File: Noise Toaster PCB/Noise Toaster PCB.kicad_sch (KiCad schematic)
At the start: 0 parts

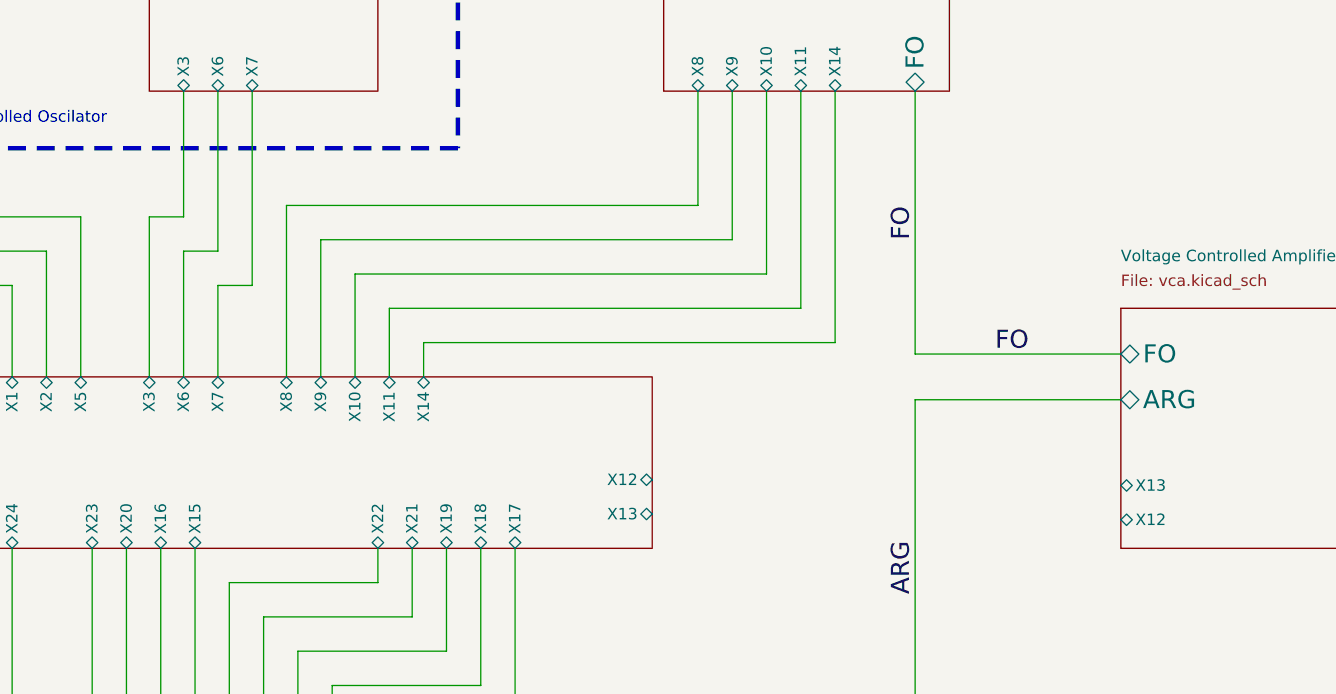
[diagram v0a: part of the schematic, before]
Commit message: wireing and components have been checked
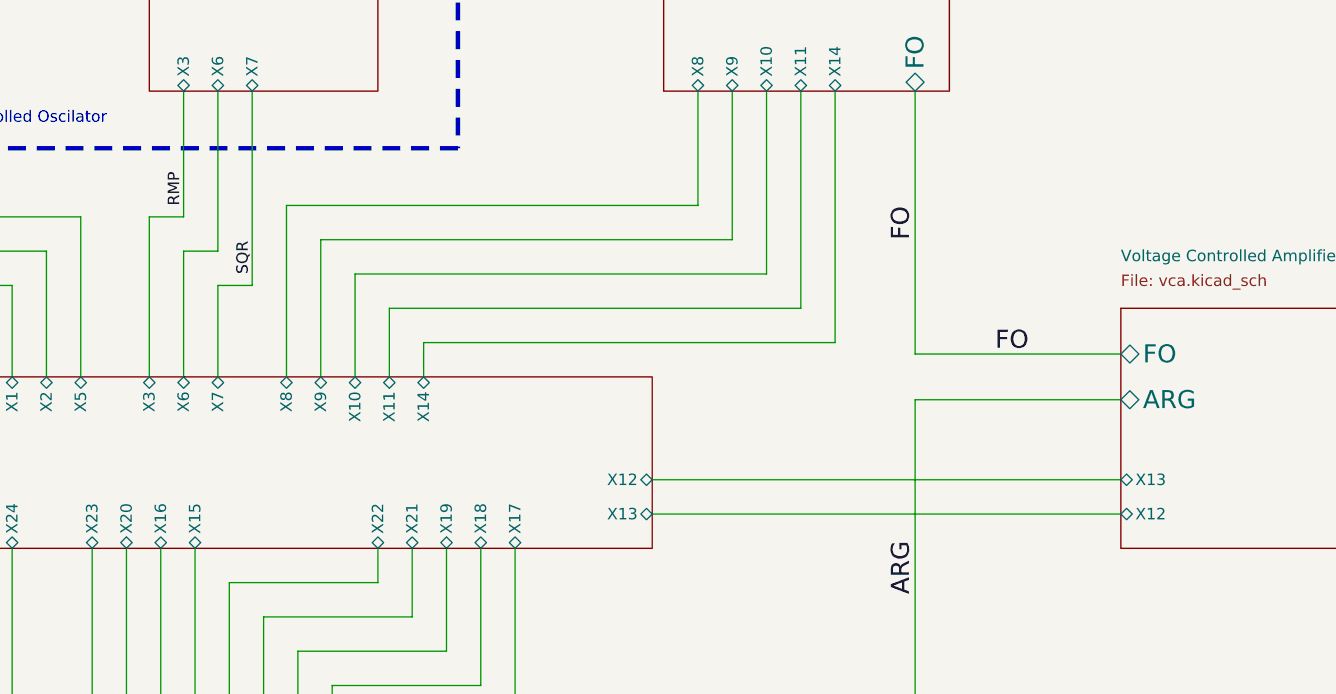
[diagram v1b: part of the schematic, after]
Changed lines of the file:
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@@
     (stroke (width 0) (type default) (color 255 157 0 1))
+  )
+  (wire (pts (xy 189.23 110.49) (xy 241.3 110.49))
+    (stroke (width 0) (type default))
   )
   (wire (pts (xy 114.3 114.3) (xy 114.3 128.27))
     (stroke (width 0) (type default) (color 255 157 0 1))
   )
+  (wire (pts (xy 144.78 63.5) (xy 144.78 85.09))
+    (stroke (width 0) (type default) (color 255 157 0 1))
+  )
   (wire (pts (xy 110.49 124.46) (xy 39.37 124.46))
     (stroke (width 0) (type default) (color 255 157 0 1))
@@
   (wire (pts (xy 194.31 76.2) (xy 194.31 63.5))
     (stroke (width 0) (type default) (color 255 157 0 1))
+  )
+  (wire (pts (xy 189.23 106.68) (xy 241.3 106.68))
+    (stroke (width 0) (type default))
   )
   (wire (pts (xy 205.74 63.5) (xy 205.74 87.63))
@@
   )
   (wire (pts (xy 127 135.89) (xy 86.36 135.89))
-    (stroke (width 0) (type default) (color 255 157 0 1))
-  )
-  (wire (pts (xy 144.78 63.5) (xy 144.78 85.09))
     (stroke (width 0) (type default) (color 255 157 0 1))
   )
@@
     (effects (font (size 2 2)) (justify left bottom))
   )
+  (label "RMP" (at 137.16 76.2 90) (fields_autoplaced)
+    (effects (font (size 1.27 1.27)) (justify left bottom))
+  )
   (label "G2" (at 118.1569 33.8641 0) (fields_autoplaced)
     (effects (font (size 2 2)) (justify left bottom))
@@
   (label "FO" (at 227.33 92.71 0) (fields_autoplaced)
     (effects (font (size 2 2)) (justify left bottom))
+  )
+  (label "SQR" (at 144.78 83.82 90) (fields_autoplaced)
+    (effects (font (size 1.27 1.27)) (justify left bottom))
   )
   (sheet (at 133.35 152.4) (size 31.75 38.1)
@@
       (effects (font (size 2 2)) (justify left))
     )
-    (pin "X13" bidirectional (at 241.3 107.315 180)
-      (effects (font (size 1.27 1.27)) (justify left))
-    )
-    (pin "X12" bidirectional (at 241.3 111.125 180)
-      (effects (font (size 1.27 1.27)) (justify left))
-    )
+    (pin "X13" bidirectional (at 241.3 106.68 180)
+      (effects (font (size 1.27 1.27)) (justify left))
+    )
+    (pin "X12" bidirectional (at 241.3 110.49 180)
+      (effects (font (size 1.27 1.27)) (justify left))
+    )

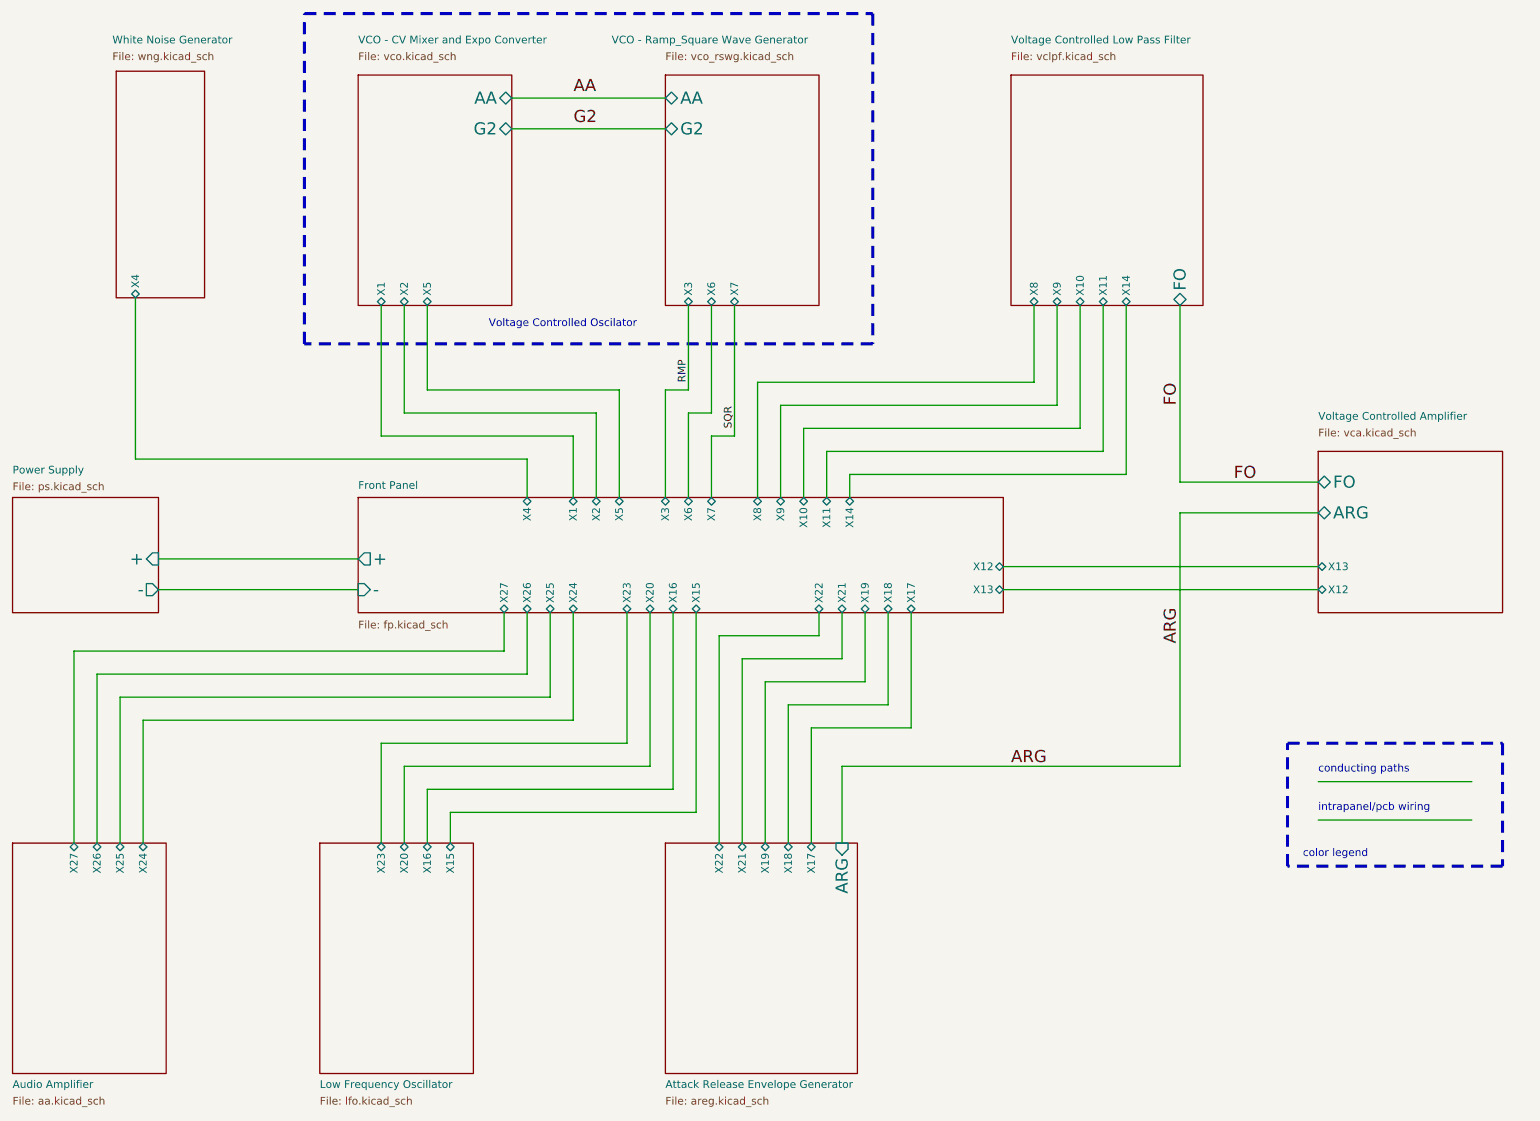
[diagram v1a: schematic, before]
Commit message: applied footprints
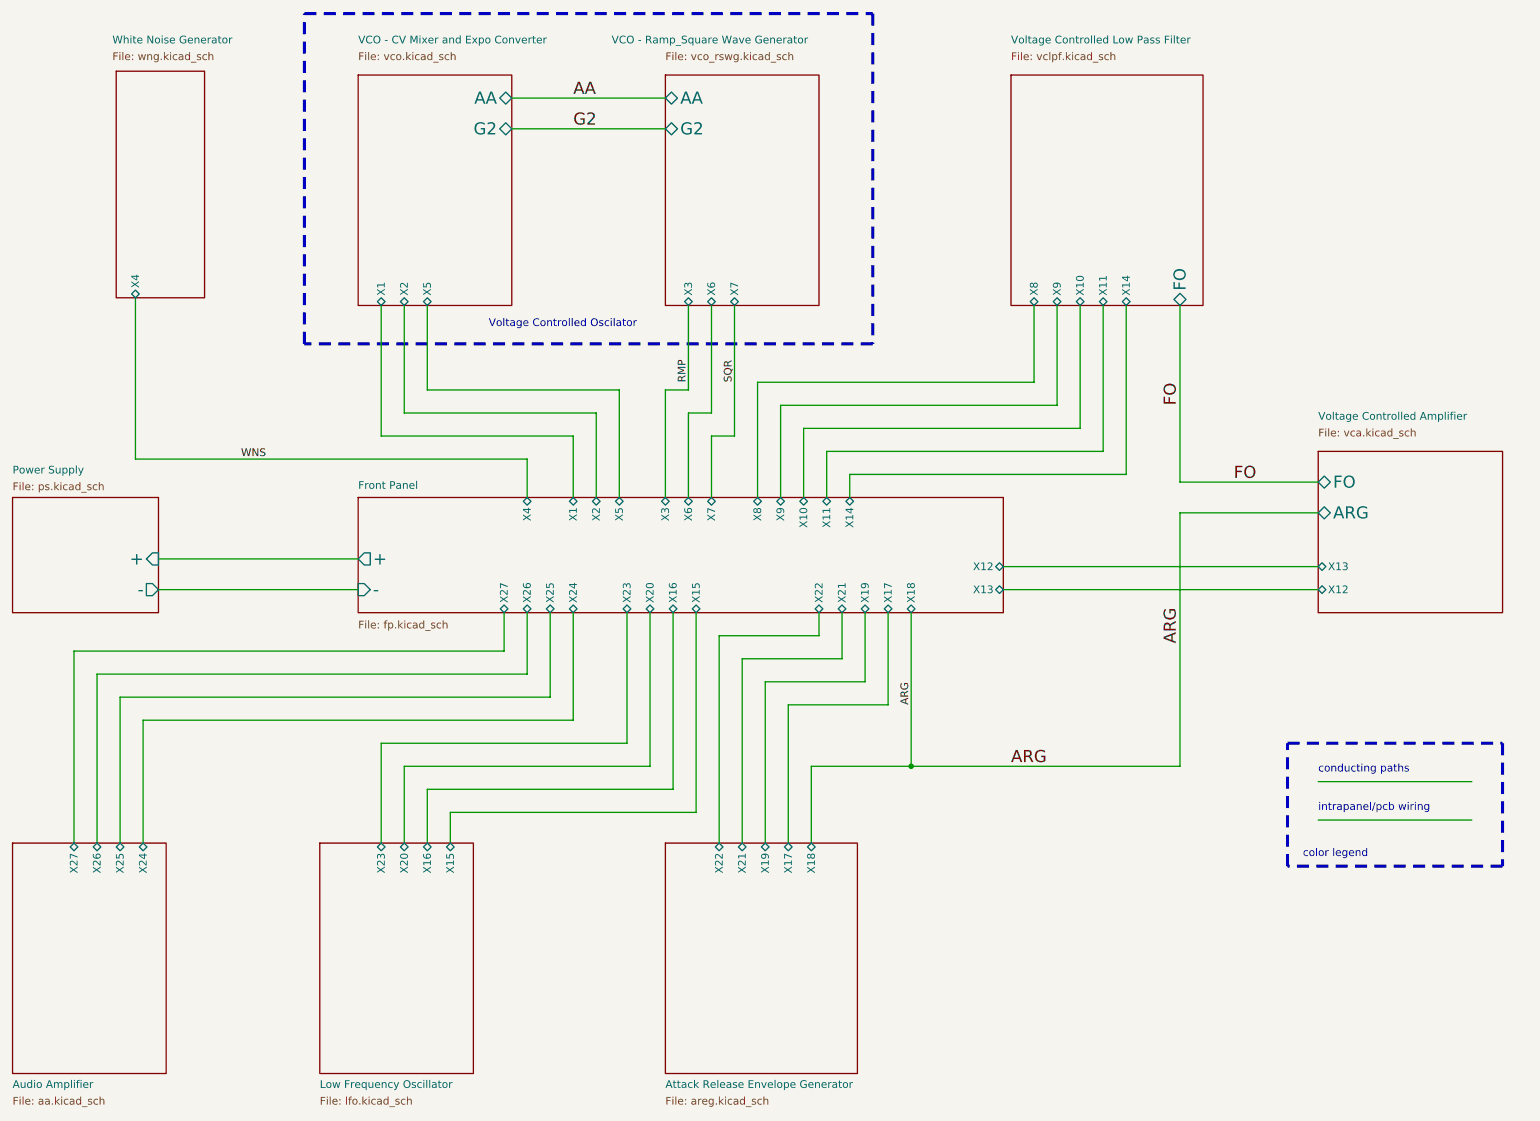
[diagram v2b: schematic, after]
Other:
- sheet Attack Release Envelope Generator ports: added none; removed ARG
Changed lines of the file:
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@@
     (comment 3 "Music From Outer Space LLC")
   )
+  (junction (at 173.99 139.7) (diameter 0) (color 0 0 0 0)
+  )
   (wire (pts (xy 114.3 128.27) (xy 43.18 128.27))
     (stroke (width 0) (type default) (color 255 157 0 1))
@@
     (stroke (width 0) (type default) (color 255 157 0 1))
   )
+  (wire (pts (xy 156.21 95.25) (xy 156.21 83.82))
+    (stroke (width 0) (type default) (color 255 157 0 1))
+  )
+  (wire (pts (xy 86.36 63.5) (xy 86.36 85.09))
+    (stroke (width 0) (type default) (color 255 157 0 1))
+  )
+  (wire (pts (xy 138.43 147.32) (xy 97.79 147.32))
+    (stroke (width 0) (type default) (color 255 157 0 1))
+  )
+  (wire (pts (xy 163.83 91.44) (xy 163.83 95.25))
+    (stroke (width 0) (type default) (color 255 157 0 1))
+  )
+  (wire (pts (xy 90.17 81.28) (xy 121.92 81.28))
+    (stroke (width 0) (type default) (color 255 157 0 1))
+  )
+  (wire (pts (xy 107.95 29.21) (xy 133.35 29.21))
+    (stroke (width 0) (type default))
+  )
+  (wire (pts (xy 173.99 139.7) (xy 218.44 139.7))
+    (stroke (width 0) (type default))
+  )
   (wire (pts (xy 153.67 129.54) (xy 153.67 152.4))
     (stroke (width 0) (type default) (color 255 157 0 1))
   )
-  (wire (pts (xy 156.21 95.25) (xy 156.21 83.82))
-    (stroke (width 0) (type default) (color 255 157 0 1))
-  )
-  (wire (pts (xy 86.36 63.5) (xy 86.36 85.09))
-    (stroke (width 0) (type default) (color 255 157 0 1))
-  )
-  (wire (pts (xy 138.43 147.32) (xy 97.79 147.32))
-    (stroke (width 0) (type default) (color 255 157 0 1))
-  )
-  (wire (pts (xy 163.83 91.44) (xy 163.83 95.25))
-    (stroke (width 0) (type default) (color 255 157 0 1))
-  )
-  (wire (pts (xy 90.17 81.28) (xy 121.92 81.28))
-    (stroke (width 0) (type default) (color 255 157 0 1))
-  )
-  (wire (pts (xy 107.95 29.21) (xy 133.35 29.21))
-    (stroke (width 0) (type default))
-  )
-  (wire (pts (xy 157.48 133.35) (xy 157.48 152.4))
-    (stroke (width 0) (type default) (color 255 157 0 1))
-  )
   (wire (pts (xy 130.81 114.3) (xy 130.81 139.7))
     (stroke (width 0) (type default) (color 255 157 0 1))
@@
     (stroke (width 0) (type default) (color 255 157 0 1))
   )
-  (wire (pts (xy 162.56 139.7) (xy 218.44 139.7))
+  (wire (pts (xy 157.48 139.7) (xy 173.99 139.7))
     (stroke (width 0) (type default))
   )
@@
     (stroke (width 0) (type default) (color 255 157 0 1))
   )
-  (wire (pts (xy 173.99 133.35) (xy 157.48 133.35))
+  (wire (pts (xy 170.18 129.54) (xy 153.67 129.54))
     (stroke (width 0) (type default) (color 255 157 0 1))
   )
@@
     (stroke (width 0) (type default) (color 255 157 0 1))
   )
-  (wire (pts (xy 173.99 114.3) (xy 173.99 133.35))
+  (wire (pts (xy 170.18 114.3) (xy 170.18 129.54))
     (stroke (width 0) (type default) (color 255 157 0 1))
   )
   (wire (pts (xy 189.23 110.49) (xy 241.3 110.49))
-    (stroke (width 0) (type default))
+    (stroke (width 0) (type default) (color 255 157 0 1))
   )
   (wire (pts (xy 114.3 114.3) (xy 114.3 128.27))
     (stroke (width 0) (type default) (color 255 157 0 1))
   )
+  (wire (pts (xy 110.49 124.46) (xy 39.37 124.46))
+    (stroke (width 0) (type default) (color 255 157 0 1))
+  )
+  (wire (pts (xy 146.05 121.92) (xy 146.05 152.4))
+    (stroke (width 0) (type default) (color 255 157 0 1))
+  )
   (wire (pts (xy 144.78 63.5) (xy 144.78 85.09))
     (stroke (width 0) (type default) (color 255 157 0 1))
   )
-  (wire (pts (xy 110.49 124.46) (xy 39.37 124.46))
-    (stroke (width 0) (type default) (color 255 157 0 1))
-  )
-  (wire (pts (xy 146.05 121.92) (xy 146.05 152.4))
-    (stroke (width 0) (type default) (color 255 157 0 1))
-  )
   (wire (pts (xy 134.62 143.51) (xy 93.98 143.51))
     (stroke (width 0) (type default) (color 255 157 0 1))
@@
   )
   (wire (pts (xy 189.23 106.68) (xy 241.3 106.68))
-    (stroke (width 0) (type default))
+    (stroke (width 0) (type default) (color 255 157 0 1))
   )
   (wire (pts (xy 205.74 63.5) (xy 205.74 87.63))
@@
     (stroke (width 0) (type default) (color 255 157 0 1))
   )
-  (wire (pts (xy 162.56 139.7) (xy 162.56 152.4))
-    (stroke (width 0) (type default))
-  )
   (wire (pts (xy 43.18 128.27) (xy 43.18 152.4))
     (stroke (width 0) (type default) (color 255 157 0 1))
@@
     (stroke (width 0) (type default) (color 255 157 0 1))
   )
-  (wire (pts (xy 170.18 129.54) (xy 153.67 129.54))
-    (stroke (width 0) (type default) (color 255 157 0 1))
-  )
   (wire (pts (xy 241.3 92.71) (xy 218.44 92.71))
     (stroke (width 0) (type default))
@@
     (stroke (width 0) (type default) (color 255 157 0 1))
   )
+  (wire (pts (xy 157.48 139.7) (xy 157.48 152.4))
+    (stroke (width 0) (type default))
+  )
   (wire (pts (xy 148.59 95.25) (xy 148.59 76.2))
     (stroke (width 0) (type default) (color 255 157 0 1))
@@
     (stroke (width 0) (type default))
   )
-  (wire (pts (xy 170.18 114.3) (xy 170.18 129.54))
+  (wire (pts (xy 173.99 114.3) (xy 173.99 139.7))
     (stroke (width 0) (type default) (color 255 157 0 1))
   )
@@
     (effects (font (size 1.27 1.27)) (justify left bottom))
   )
-  (label "G2" (at 118.1569 33.8641 0) (fields_autoplaced)
-    (effects (font (size 2 2)) (justify left bottom))
-  )
-  (label "AA" (at 118.1521 28.7399 0) (fields_autoplaced)
+  (label "G2" (at 118.11 34.29 0) (fields_autoplaced)
+    (effects (font (size 2 2)) (justify left bottom))
+  )
+  (label "AA" (at 118.11 29.21 0) (fields_autoplaced)
     (effects (font (size 2 2)) (justify left bottom))
   )
@@
     (effects (font (size 2 2)) (justify left bottom))
   )
-  (label "SQR" (at 144.78 83.82 90) (fields_autoplaced)
-    (effects (font (size 1.27 1.27)) (justify left bottom))
+  (label "SQR" (at 144.78 76.2 90) (fields_autoplaced)
+    (effects (font (size 1.27 1.27)) (justify left bottom))
+  )
+  (label "ARG" (at 173.99 129.54 90) (fields_autoplaced)
+    (effects (font (size 1.27 1.27)) (justify left bottom))
+  )
+  (label "WNS" (at 67.31 88.9 180) (fields_autoplaced)
+    (effects (font (size 1.27 1.27)) (justify right bottom))
   )
   (sheet (at 133.35 152.4) (size 31.75 38.1)
@@
       (effects (font (size 1.27 1.27)) (justify left top))
     )
-    (pin "X18" bidirectional (at 153.67 152.4 90)
+    (pin "X18" bidirectional (at 157.48 152.4 90)
       (effects (font (size 1.27 1.27)) (justify right))
     )
@@
       (effects (font (size 1.27 1.27)) (justify right))
     )
-    (pin "ARG" input (at 162.56 152.4 90)
-      (effects (font (size 2 2)) (justify right))
-    )
-    (pin "X17" bidirectional (at 157.48 152.4 90)
+    (pin "X17" bidirectional (at 153.67 152.4 90)
       (effects (font (size 1.27 1.27)) (justify right))
     )
@@
       (effects (font (size 1.27 1.27)) (justify left top))
     )
-    (pin "X17" bidirectional (at 173.99 114.3 270)
+    (pin "X17" bidirectional (at 170.18 114.3 270)
       (effects (font (size 1.27 1.27)) (justify left))
     )
-    (pin "X18" bidirectional (at 170.18 114.3 270)
+    (pin "X18" bidirectional (at 173.99 114.3 270)
       (effects (font (size 1.27 1.27)) (justify left))
     )

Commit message: placed pards of the pcb properly
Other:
- company: http://musicfromouterspace.com/analogsynth_new/NOISETOASTER/NOISETOASTER.php -> Music From Outer Space LLC
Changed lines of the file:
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@@
     (title "Noise Toaster")
     (rev "0.5")
-    (company "http://musicfromouterspace.com/analogsynth_new/NOISETOASTER/NOISETOASTER.php")
+    (company "Music From Outer Space LLC")
     (comment 1 "Licence: CC-BY-NC-SA")
     (comment 2 "Original Design by Ray Wilson")
-    (comment 3 "Music From Outer Space LLC")
+    (comment 3 "http://musicfromouterspace.com/analogsynth_new/NOISETOASTER/NOISETOASTER.php")
   )
   (junction (at 173.99 139.7) (diameter 0) (color 0 0 0 0)
